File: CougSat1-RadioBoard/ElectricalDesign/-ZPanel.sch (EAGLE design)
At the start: 19 parts, among them J1 High Gain Antenna, J2 Deployables, J3 High Gain +, J4 ADCS, J5 Flap +X, J6 Flap -X, J7 Flap +Y, J8 Flap -Y, U1 LTC2499

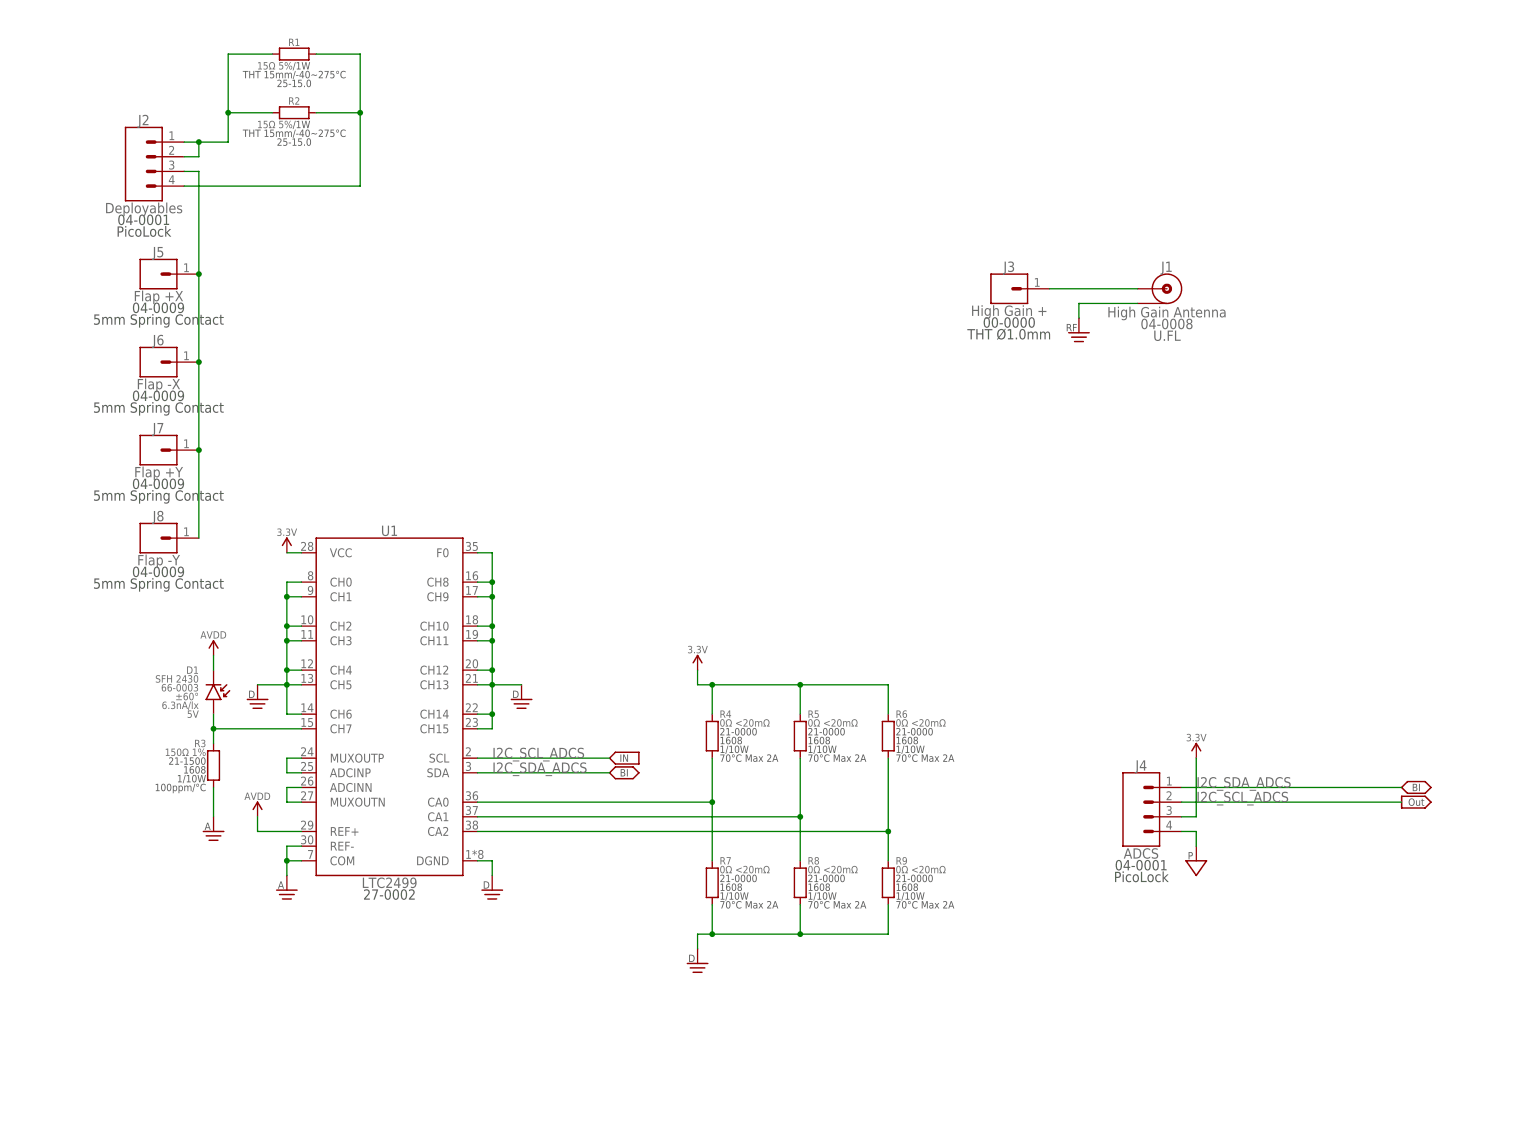
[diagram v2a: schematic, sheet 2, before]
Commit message: Revision 1.1
Made changes to fix errors listed for design document and schematic
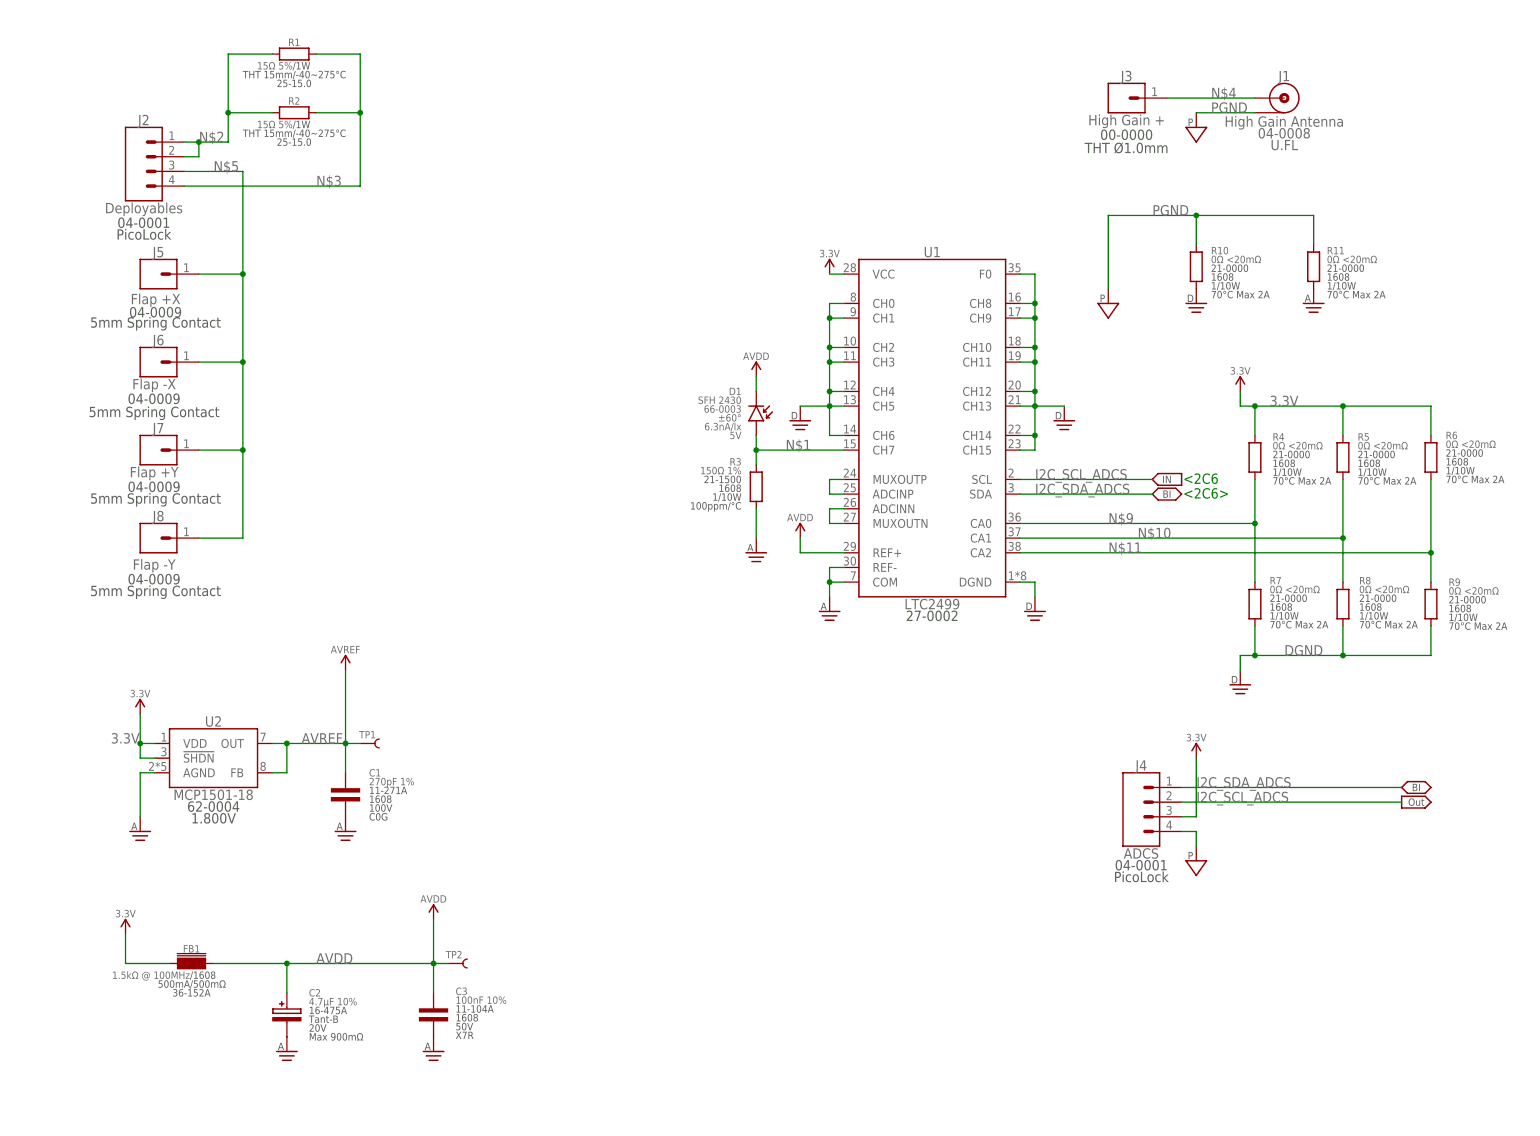
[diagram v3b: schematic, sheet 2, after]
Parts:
- added C1: 270pF 1%, CougsInSpace-Capacitors:CAP-V-270PF-1608
- added C2: 4.7µF 10%, CougsInSpace-Capacitors:CAP-POL-V-4.7UF-4028
- added C3: 100nF 10%, CougsInSpace-Capacitors:CAP-V-100NF-1608
- added FB1: 1.5kΩ @ 100MHz, CougsInSpace-Coils:CHOKE-H-1.5K-1608
- added R10, R11: 0Ω <20mΩ, CougsInSpace-Resistors:RES-V-0-1608
- added TP1, TP2: TEST_POINT-THT-0.7, CougsInSpace-Connectors:TEST_POINT-THT-0.7
- added U2: MCP1501-18, CougsInSpace-IC-Other:MCP1501-18E/RW
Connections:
- removed net RFGND: J1.SHIELD
- new net AVREF: C1.1, TP1.1, U2.FB, U2.OUT
- net 3.3V: now also FB1.1, U2.!SHDN, U2.VDD
- net AGND: now also C1.2, C2.C, C3.2, R11.1, U2.AGND
- net AVDD: now also C2.A, C3.1, FB1.2, TP2.1
- net DGND: now also R10.1
- net PGND: now also J1.SHIELD, R10.2, R11.2
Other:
- note added: "<2C6"
- note added: "<2C6>"
- moved on the sheet: D1, J1, J3, R3, R4, R5, R6, R7, R8, R9, U1

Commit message: Update -ZPanel.sch
Ready for re-review
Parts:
- removed R4, R5, R6, R7, R8, R9: 0Ω <20mΩ, CougsInSpace-Resistors:RES-V-0-1608
- added C4: 1µF 10%, CougsInSpace-Capacitors:CAP-V-1UF-1608
- added C5: 10µF 10%, CougsInSpace-Capacitors:CAP-V-10UF-1608
- added R12: 1kΩ 0.1%, CougsInSpace-Resistors:RES-H-1K-1608
- added U3: AD8515, CougsInSpace-IC-Amplifiers:OPAMP-1-AD8515
- U1: value LTC2499 -> AD7291; device CougsInSpace-IC-Conversion:LTC2499 -> CougsInSpace-IC-Conversion:AD7291
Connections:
- removed net N$10: R5.1, R8.2, U1.CA1
- removed net N$11: R6.1, R9.2, U1.CA2
- removed net N$7: U1.ADCINN, U1.MUXOUTN
- new net N$8: C4.1, U1.DCAP
- net 3.3V: now also R12.2, U1.AS0, U1.VDRIVE; no longer R4.2, R5.2, R6.2, U1.VCC
- net AGND: now also C4.2, C5.2, U1.AGND, U3.V-; no longer U1.COM, U1.REF-
- net AVDD: now also U1.VDD, U3.V+; no longer U1.REF+
- net AVREF: now also U3.IN-, U3.OUT
- net DGND: now also U1.AS1, U1.IN1, U1.IN2, U1.IN3, U1.IN4, U1.IN5, U1.IN6, U1.IN7; no longer R7.1, R8.1, R9.1, U1.CH0, U1.CH1, U1.CH10, U1.CH11, U1.CH12, U1.CH13, U1.CH14, U1.CH15, U1.CH2, U1.CH3, U1.CH4, U1.CH5, U1.CH6, U1.CH8, U1.CH9, U1.F0
- net N$1: now also U1.IN0; no longer U1.CH7
- net N$6: now also R12.1, U1.!PD!/!RST; no longer U1.ADCINP, U1.MUXOUTP
- net N$9: now also C5.1, U1.VREF, U3.IN+; no longer R4.1, R7.2, U1.CA0
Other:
- moved on the sheet: D1, R3

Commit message: Ready For Review
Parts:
- removed TP1: TEST_POINT-THT-0.7, CougsInSpace-Connectors:TEST_POINT-THT-0.7
- removed U2: MCP1501-18, CougsInSpace-IC-Other:MCP1501-18E/RW
- added C6, C7, C8: 100nF 10%, CougsInSpace-Capacitors:CAP-V-100NF-1608
- added H1, H2, H3, H4: M3, CougsInSpace-Hardware:MOUNTING_HOLE-3.3
- added R4, R5, R6, R7: 0Ω <20mΩ, CougsInSpace-Resistors:RES-V-0-1608
- added RN1, RN2: 10kΩ 1%, CougsInSpace-Resistors:RES-4-V-10K-1632
- added RT1, RT2, RT3, RT4, RT5, RT6, RT7: 10kΩ 5%, CougsInSpace-Resistors:THERMISTOR-V-10K-1608
- C1: value 270pF 1% -> 100nF 10%; device CougsInSpace-Capacitors:CAP-V-270PF-1608 -> CougsInSpace-Capacitors:CAP-V-100NF-1608
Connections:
- net N$1 renamed PHOTODIO_ADC
- net N$2 renamed DEPLOY-H
- net N$4 renamed HIGH_G_1
- net N$5 renamed SPRING_CONTACT
- removed net N$3: J2.4, R1.2, R2.2
- new net CHASSIS: C1.1, C6.1, C7.1, C8.1, H1.MOUNT, H2.MOUNT, H3.MOUNT, H4.MOUNT, R4.2, R5.2, R6.2, R7.2
- new net RFGND: J1.SHIELD
- new net THERM-0: RN1A.1, RT1.2, U1.IN1
- new net THERM-1: RN1B.1, RT2.2, U1.IN2
- new net THERM-2: RN1C.1, RT3.2, U1.IN3
- new net THERM-3: RN1D.1, RT4.2, U1.IN4
- new net THERM-4: RN2A.1, RT5.2, U1.IN5
- new net THERM-5: RN2B.1, RT6.2, U1.IN6
- new net THERM-6: RN2C.1, RT7.2, U1.IN7
- net 3.3V: no longer U2.!SHDN, U2.VDD
- net AGND: now also RT1.1, RT2.1, RT3.1, RT4.1, RT5.1, RT6.1, RT7.1; no longer C1.2, U2.AGND
- net AVREF: now also RN1A.2, RN1B.2, RN1C.2, RN1D.2, RN2A.2, RN2B.2, RN2C.2; no longer C1.1, TP1.1, U2.FB, U2.OUT
- net DGND: no longer U1.IN1, U1.IN2, U1.IN3, U1.IN4, U1.IN5, U1.IN6, U1.IN7
- net PGND: now also C1.2, C6.2, C7.2, C8.2, J2.4, R1.2, R2.2, R4.1, R5.1, R6.1, R7.1; no longer J1.SHIELD
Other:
- note added: "<2A1"
- note added: "<2C2"
- note added: "Page 1: Block Diagram Page 2: Electrical Schematic Page 3: Mechanical"
- note removed: "<2C6"
- note removed: "<2C6>"
- note removed: "Page 1: Block Diagram"
- moved on the sheet: C1, C2, C3, C4, C5, D1, FB1, J2, J4, J5, J6, J7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

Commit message: Ready For Review
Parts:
- added C11, C12, C9: 100nF 10%, CougsInSpace-Capacitors:CAP-V-100NF-1608
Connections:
- net N$6 renamed PD/RST
- net N$8 renamed DCAP
- net N$9 renamed VREF
- net 3.3V: now also C12.1
- net AGND: now also C11.2, C9.2
- net AVDD: now also C11.1, C9.1
- net DGND: now also C12.2
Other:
- note added: "96mm"
- note added: "CAD Note: ADC Address: 10"
- note added: "CAD Note: Center Point"
- note added: "CAD Note: Decoupling"
- note removed: "<2C2"
- moved on the sheet: J4

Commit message: 1.0.3
Ready for review
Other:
- note added: "ADC Address: 10"
- note removed: "CAD Note: ADC Address: 10"
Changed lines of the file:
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@@
 <setting verticaltext="up"/>
 </settings>
-<grid distance="1" unitdist="mm" unit="mm" style="lines" multiple="1" display="yes" altdistance="1" altunitdist="mm" altunit="mm"/>
+<grid distance="0.1" unitdist="inch" unit="inch" style="lines" multiple="1" display="no" altdistance="0.01" altunitdist="inch" altunit="inch"/>
 <layers>
 <layer number="1" name="Top" color="4" fill="1" visible="no" active="no"/>
@@
 <wire x1="78.74" y1="106.68" x2="78.74" y2="129.54" width="0.1524" layer="97" style="shortdash"/>
 <wire x1="78.74" y1="129.54" x2="50.8" y2="129.54" width="0.1524" layer="97" style="shortdash"/>
-<text x="40.64" y="182.88" size="1.778" layer="97">CAD Note: ADC Address: 10</text>
+<text x="40.64" y="182.88" size="1.778" layer="97">ADC Address: 10</text>
 </plain>
 <instances>

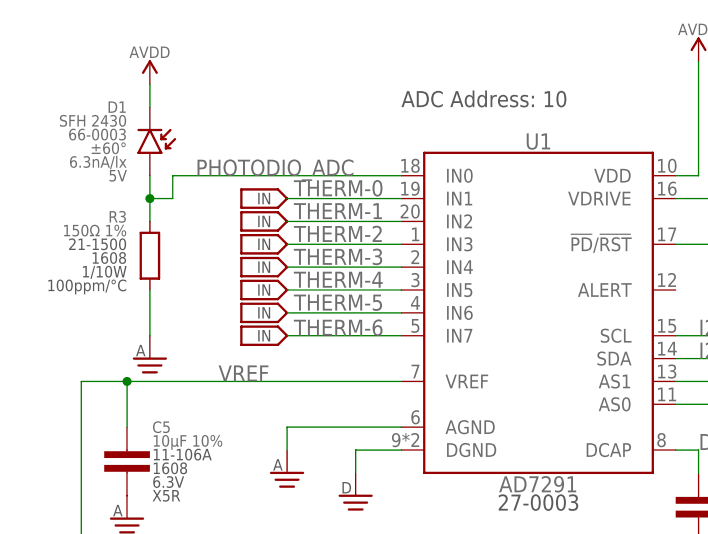
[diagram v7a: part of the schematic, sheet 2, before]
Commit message: Finished items listed
Comments:
-Gabe verified AS1 low AS0 high
-Unsure about section 3 formatting
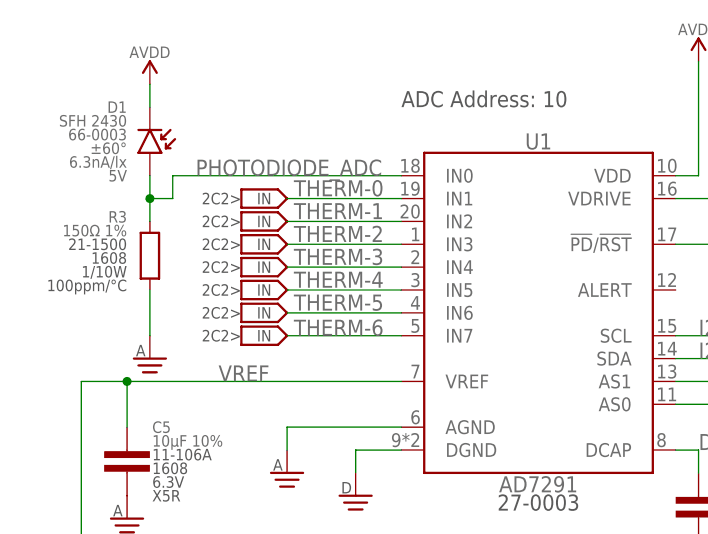
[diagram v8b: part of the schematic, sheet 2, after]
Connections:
- net PHOTODIO_ADC renamed PHOTODIODE_ADC
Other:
- note added: "2C2>"
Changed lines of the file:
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@@
 <sheet>
 <plain>
-<text x="22.86" y="172.72" size="1.27" layer="97" align="center-right">&gt;2C2  </text>
-<text x="22.86" y="170.18" size="1.27" layer="97" align="center-right">&gt;2C2  </text>
-<text x="22.86" y="167.64" size="1.27" layer="97" align="center-right">&gt;2C2  </text>
-<text x="22.86" y="165.1" size="1.27" layer="97" align="center-right">&gt;2C2  </text>
-<text x="22.86" y="162.56" size="1.27" layer="97" align="center-right">&gt;2C2  </text>
-<text x="22.86" y="160.02" size="1.27" layer="97" align="center-right">&gt;2C2  </text>
-<text x="22.86" y="157.48" size="1.27" layer="97" align="center-right">&gt;2C2  </text>
+<text x="22.86" y="172.72" size="1.27" layer="97" align="center-right">2C2&gt;  </text>
+<text x="22.86" y="170.18" size="1.27" layer="97" align="center-right">2C2&gt;  </text>
+<text x="22.86" y="167.64" size="1.27" layer="97" align="center-right">2C2&gt;  </text>
+<text x="22.86" y="165.1" size="1.27" layer="97" align="center-right">2C2&gt;  </text>
+<text x="22.86" y="162.56" size="1.27" layer="97" align="center-right">2C2&gt;  </text>
+<text x="22.86" y="160.02" size="1.27" layer="97" align="center-right">2C2&gt;  </text>
+<text x="22.86" y="157.48" size="1.27" layer="97" align="center-right">2C2&gt;  </text>
 <text x="68.58" y="88.9" size="1.27" layer="97" align="center-right">&lt;2A1 </text>
 <text x="68.58" y="86.36" size="1.27" layer="97" align="center-right">&lt;2A1 </text>
@@
 </segment>
 </net>
-<net name="PHOTODIO_ADC" class="0">
+<net name="PHOTODIODE_ADC" class="0">
 <segment>
 <pinref part="U1" gate="G$1" pin="IN0"/>
